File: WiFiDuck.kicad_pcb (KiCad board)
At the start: 2 copper layers, 21.2 x 30 mm, 12 parts, among them J1 USB_A, J2 DEBUG, U1 ESP-12F, U2 CH9328, U3 AMS1117-3.3

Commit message: v0.2.0
Fix CH9328 footprint
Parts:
- U2: footprint Package_DIP:DIP-16_W7.62mm_SMDSocket_SmallPads -> Package_SO:SOP-16_3.9x9.9mm_P1.27mm
- moved J1 0.09 mm to (109.2, 118.2)
- turned R2 to 180 degrees
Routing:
- net Net-(U1-CH_PD): track 10.2 -> 4.86 mm
- net +3.3V: track 63.6 -> 68.3 mm
- net GND: track 71.6 -> 69.5 mm
- net Net-(U1-GPIO15): track 15.9 -> 13.8 mm
- net Net-(U2-IO2): track 4.55 -> 5.89 mm
- net /RXD: track 19.1 -> 20.1 mm

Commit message: Add JLC customer number
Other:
- board text added: "JLCJLCJLCJLC"
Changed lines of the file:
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@@
   (gr_rect (start 98.59 82.4) (end 119.79 112.4)
     (stroke (width 0.1) (type default)) (fill none) (layer "Edge.Cuts"))
+  (gr_text "JLCJLCJLCJLC" (at 113.449286 93.32875) (layer "B.SilkS")
+    (effects (font (size 0.8 0.8) (thickness 0.15) bold) (justify left bottom mirror))
+  )
   (gr_text "GND" (at 115.08 106.6) (layer "F.SilkS")
     (effects (font (size 0.8 0.8) (thickness 0.15) bold) (justify bottom))

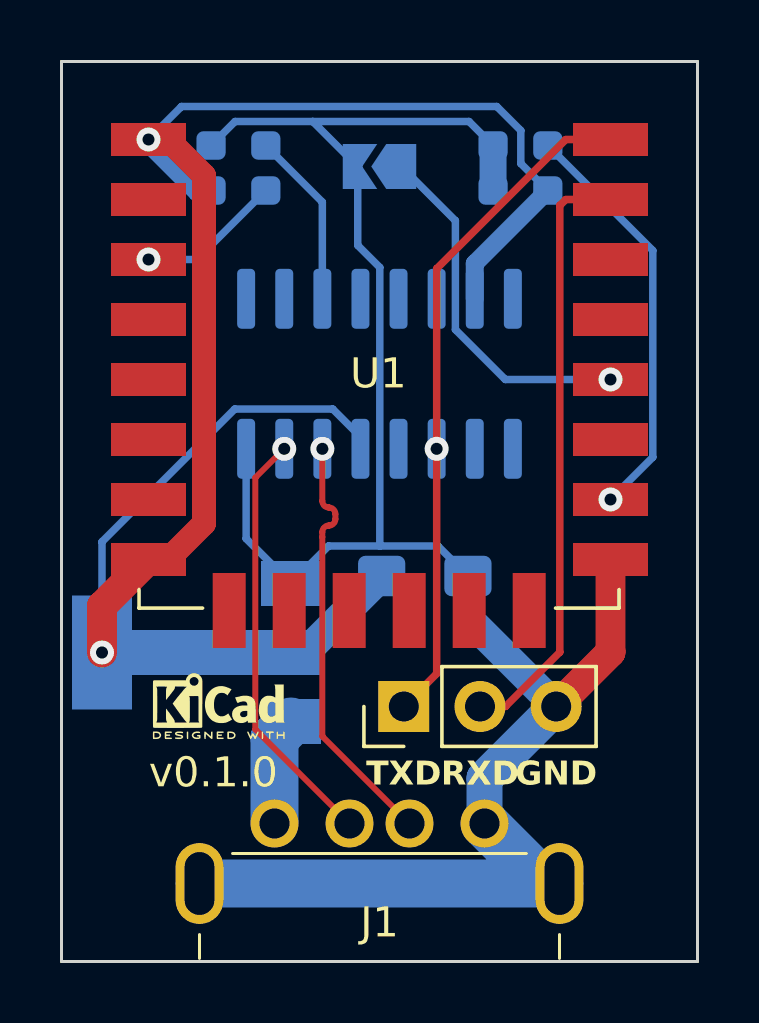
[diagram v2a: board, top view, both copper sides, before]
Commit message: v0.3.0
Fix USB-A
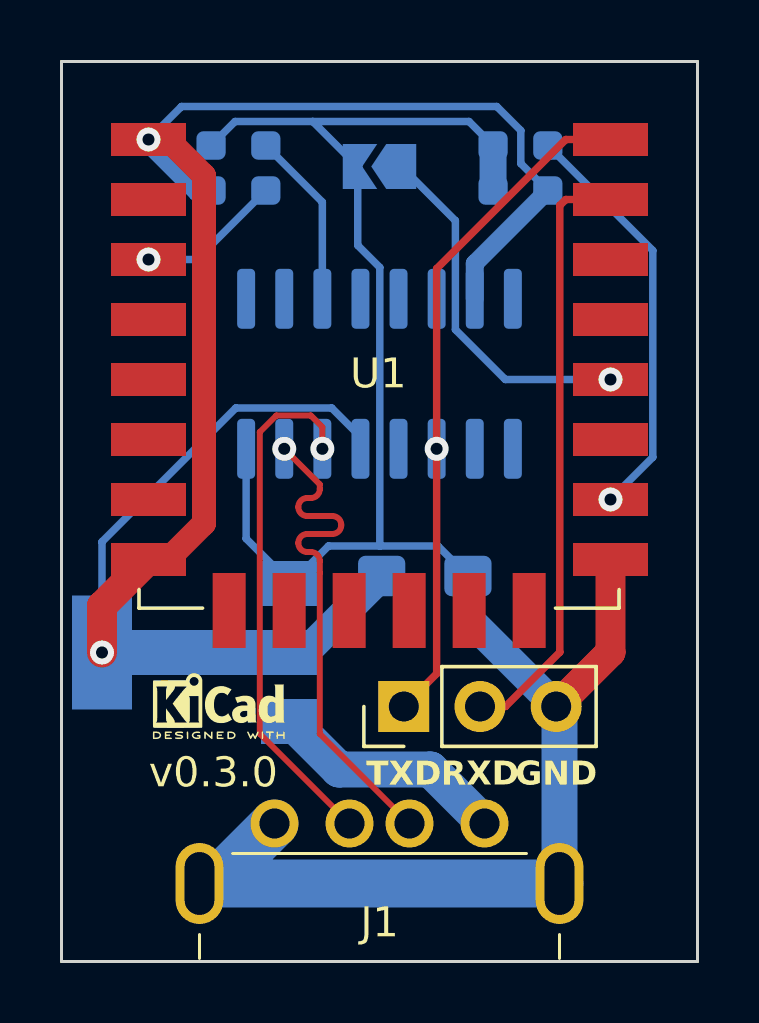
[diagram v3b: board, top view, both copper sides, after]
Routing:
- net +5V: track 3.63 -> 7.86 mm
- net /DP: track 14.2 -> 17.5 mm
- net /DN: track 14.2 -> 17.4 mm
- net GND: track 69.5 -> 70.1 mm
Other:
- board text added: "v0.3.0"
- board text removed: "v0.1.0"
